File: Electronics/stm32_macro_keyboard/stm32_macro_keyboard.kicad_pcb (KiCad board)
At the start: 2 copper layers, 120.4 x 59.9 mm, 37 parts, among them J1 USB_B_Micro, J2 Conn_01x04_Pin, SW1 SW_SPDT, U1 STM32F072CBTx, U2 AMS1117-3.3, Y1 16 MHz

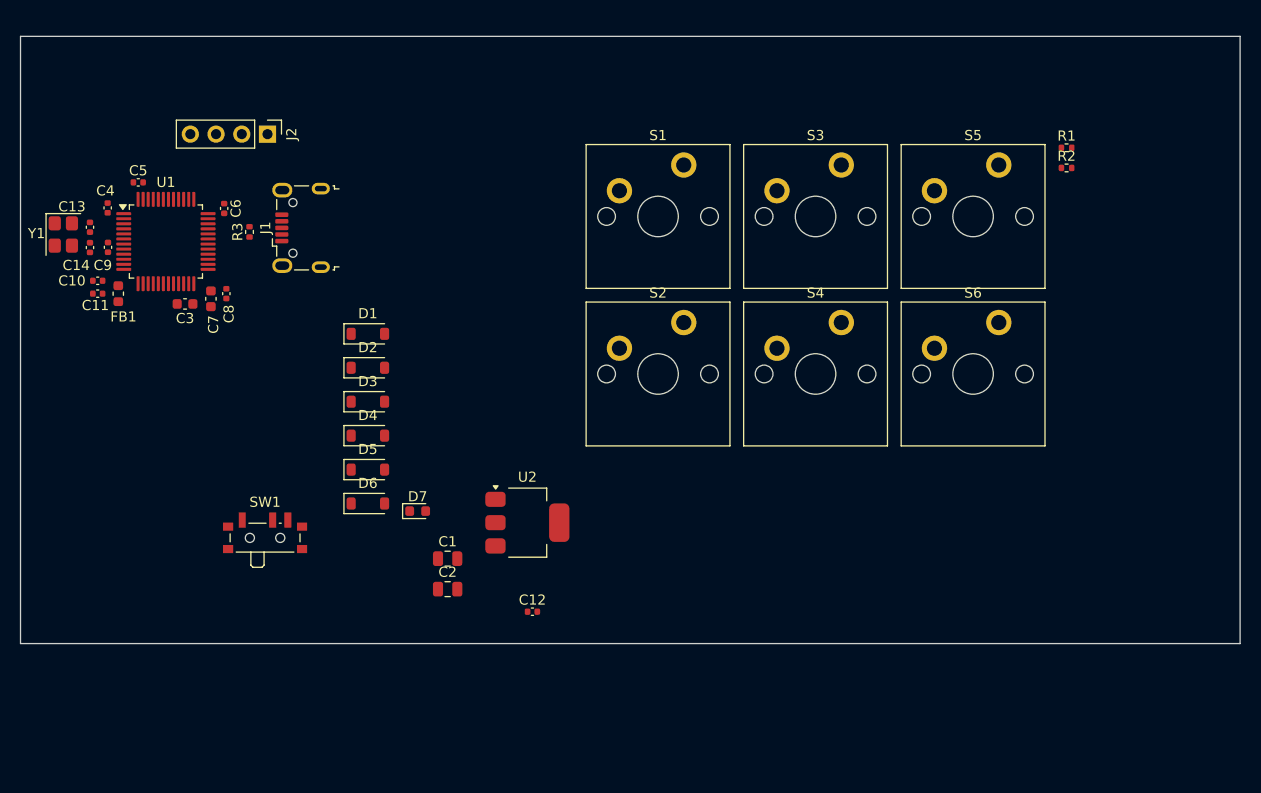
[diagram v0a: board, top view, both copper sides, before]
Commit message: Configure copper zone fill settings and add mounting holes to PCB layout
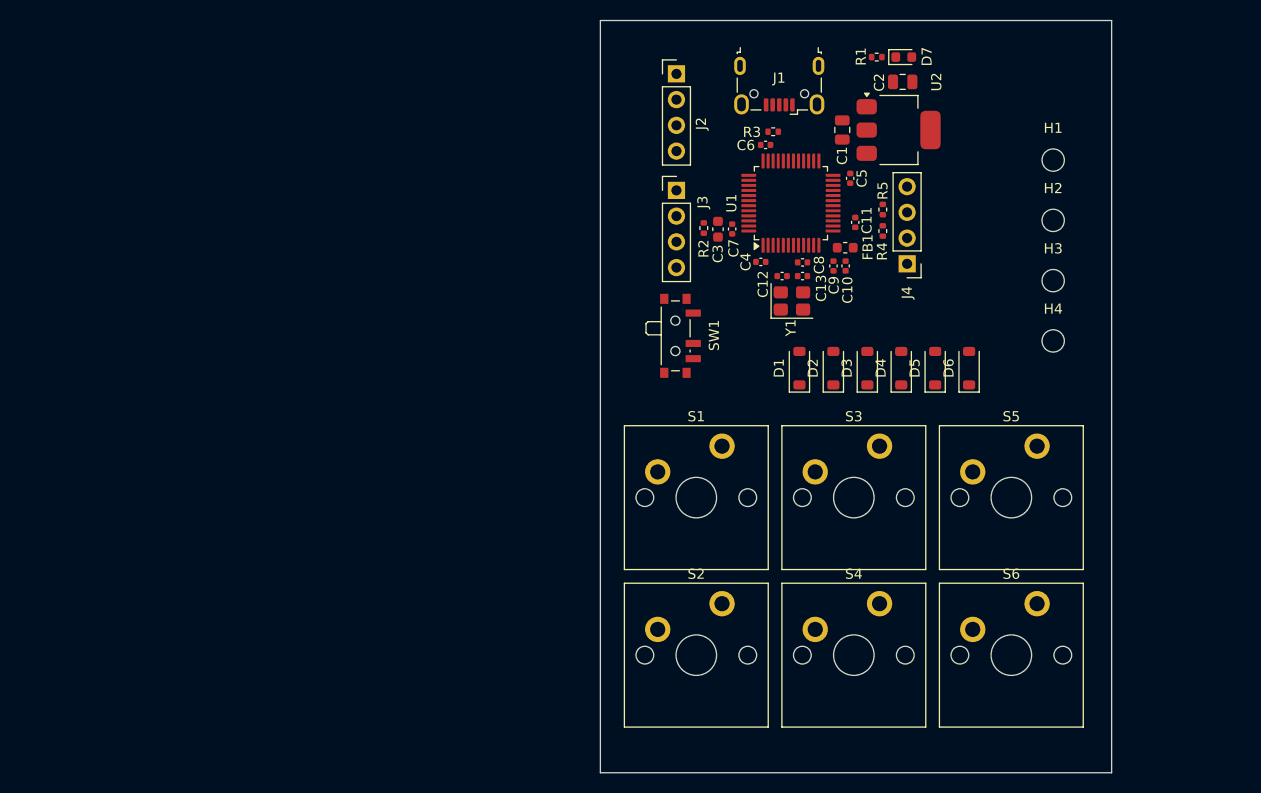
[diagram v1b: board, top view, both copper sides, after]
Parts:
- removed C14: 10p, Capacitor_SMD:C_0402_1005Metric
- added H1: MountingHole, MountingHole:MountingHole_2.2mm_M2, F.Cu at (158.8, 49.3)
- added H2: MountingHole, MountingHole:MountingHole_2.2mm_M2, F.Cu at (158.8, 55.2)
- added H3: MountingHole, MountingHole:MountingHole_2.2mm_M2, F.Cu at (158.8, 61.2)
- added H4: MountingHole, MountingHole:MountingHole_2.2mm_M2, F.Cu at (158.8, 67.2)
- added J3: Conn_01x04_Pin, Connector_PinHeader_2.54mm:PinHeader_1x04_P2.54mm_Vertical, F.Cu at (121.7, 52.3)
- added J4: Conn_01x04_Pin, Connector_PinHeader_2.54mm:PinHeader_1x04_P2.54mm_Vertical, F.Cu at (144.4, 59.5)
- added R4: 1k5, Resistor_SMD:R_0402_1005Metric, F.Cu at (142.0, 56.3)
- added R5: 1k5, Resistor_SMD:R_0402_1005Metric, F.Cu at (142.0, 54.2)
- C11: value 1u -> 100n
- C12: value 100n -> 10p
- C3: value 4.7u -> 10u
- C7: value 4.7u -> 100n; footprint Capacitor_SMD:C_0603_1608Metric -> Capacitor_SMD:C_0402_1005Metric
- C8: value 100n -> 10n
- C9: value 10n -> 1u
- D7: value LED -> RED
- U1: value STM32F072CBTx -> STM32F103C8T6
- Y1: value 16 MHz -> 16MHz
- moved C11 75.1 mm to (139.3, 55.5), turned to 90 degrees
- moved C10 73.8 mm to (138.3, 59.8), turned to -90 degrees
- moved Y1 72.2 mm to (133.1, 63.2), turned to 0 degrees
- moved FB1 71.9 mm to (138.3, 58.0), turned to 0 degrees
- moved C9 71.6 mm to (137.2, 59.8), turned to -90 degrees
- moved C13 70.5 mm to (134.1, 60.8), turned to 180 degrees
- moved C5 70.3 mm to (138.8, 51.1), turned to -90 degrees
- moved C2 67.3 mm to (144.0, 41.6), turned to 180 degrees
- moved D7 65.7 mm to (144.1, 39.1)
- moved C4 64.7 mm to (130.0, 59.4), turned to 180 degrees
- moved U1 61.8 mm to (132.9, 53.5), turned to 90 degrees
- moved D6 60.8 mm to (150.5, 69.8), turned to 90 degrees
- moved C1 57.5 mm to (138.0, 46.3), turned to 90 degrees
- moved C8 57.0 mm to (134.1, 59.4), turned to 0 degrees
- moved D5 56.9 mm to (147.2, 69.8), turned to 90 degrees
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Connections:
- C10 pad 1: +3.3VA -> +3.3V
- C11 pad 1: +3.3V -> /NRST
- C12 pad 1: /NRST -> /HSE_IN
- C13 pad 1: /HSE_IN -> /HSE_OUT
- C8 pad 1: +3.3V -> +3.3VA
- U1 pad 10: unconnected-(U1-PA0-Pad10) -> Row 1
- U1 pad 11: unconnected-(U1-PA1-Pad11) -> Row 2
- U1 pad 12: unconnected-(U1-PA2-Pad12) -> Col 1
- U1 pad 13: Row 1 -> Col 2
- U1 pad 14: Row 2 -> Col 3
- U1 pad 15: Col 1 -> unconnected-(U1-PA5-Pad15)
- U1 pad 16: Col 2 -> unconnected-(U1-PA6-Pad16)
- U1 pad 17: Col 3 -> unconnected-(U1-PA7-Pad17)
- U1 pad 21: unconnected-(U1-PB10-Pad21) -> /I2C2_SCL
- U1 pad 22: unconnected-(U1-PB11-Pad22) -> /I2C2_SDA
- U1 pad 42: unconnected-(U1-PB6-Pad42) -> /USART1_TX
- U1 pad 43: unconnected-(U1-PB7-Pad43) -> /USART1_RX
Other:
- board size 120.4 x 59.9 mm -> 50.5 x 74.3 mm
